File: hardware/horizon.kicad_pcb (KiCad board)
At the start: 4 copper layers, 106.9 x 56.2 mm, 62 parts, among them J1 Conn_01x02_Pin, J2 Conn_01x06_Pin, J3 USB_C_Receptacle_USB2.0_14P, J4 Conn_01x14_Pin, J5 Conn_01x02_Socket, J6 Conn_01x02_Pin, J7 SD_Card_Receptacle, Q1 NPN, SW1 SW_Push, SW2 SW_Push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

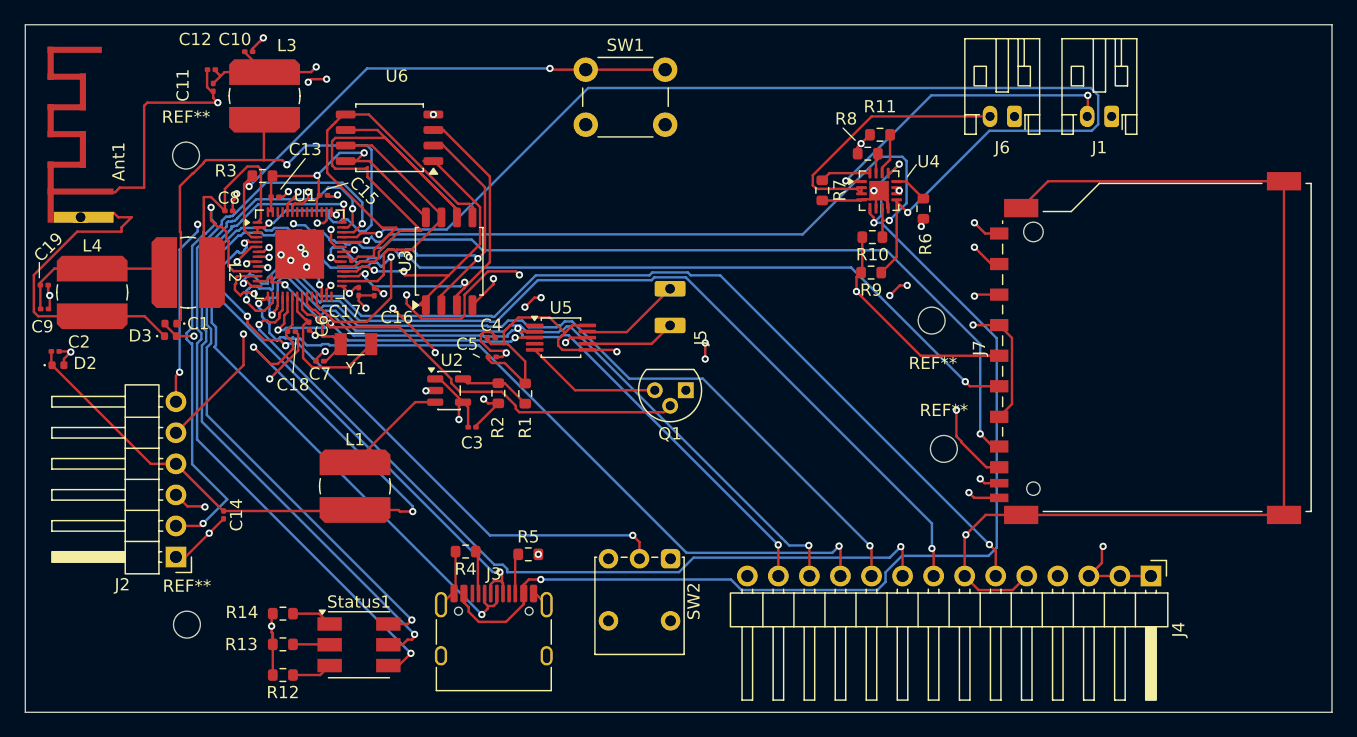
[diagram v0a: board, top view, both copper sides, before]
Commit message: Fixed connectors
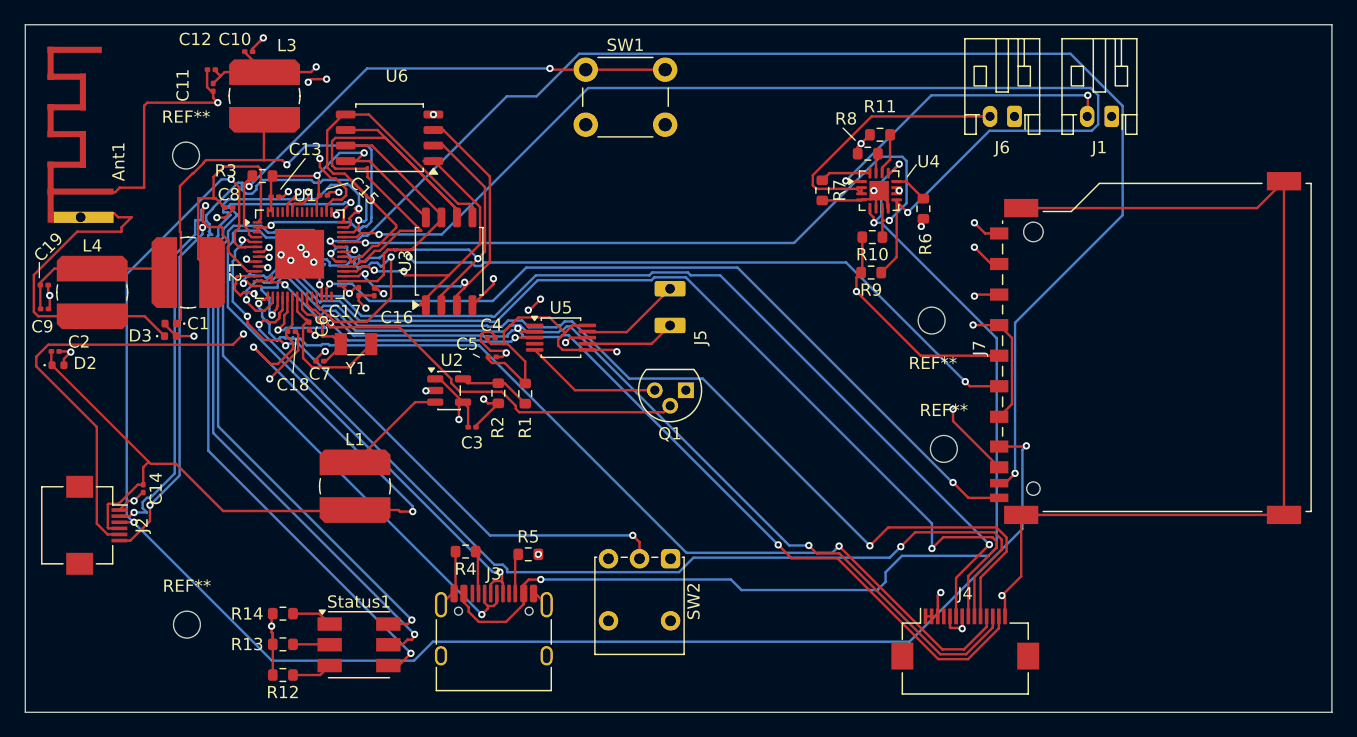
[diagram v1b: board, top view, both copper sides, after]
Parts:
- J2: footprint Connector_PinHeader_2.54mm:PinHeader_1x06_P2.54mm_Horizontal -> Connector_FFC-FPC:Hirose_FH12-6S-0.5SH_1x06-1MP_P0.50mm_Horizontal
- J4: footprint Connector_PinHeader_2.54mm:PinHeader_1x14_P2.54mm_Horizontal -> Connector_FFC-FPC:Hirose_FH12-14S-0.5SH_1x14-1MP_P0.50mm_Horizontal
- moved J4 16.0 mm to (178.5, 101.0), turned to 0 degrees
- moved J2 6.97 mm to (107.5, 91.8), turned to -90 degrees
- moved C14 6.92 mm to (111.2, 88.8)
- moved C8 0.28 mm to (118.2, 65.8)
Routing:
- net SDCARD_DAT0: track 78.5 -> 131.0 mm, vias 3 -> 2
- net +5V: track 125.1 -> 92.4 mm
- net Touch-SCL: track 18.5 -> 43.8 mm
- net SPI_HOSTHRDY: track 56.1 -> 77.5 mm
- net SPI_CLK: track 66.4 -> 84.5 mm
- net SPI_RESET: track 58.6 -> 76.6 mm
- net SPI_CS0: track 61.1 -> 75.8 mm
- net SPI_MISO: track 68.5 -> 82.4 mm
- net SPI_MOSI: track 77.5 -> 87.7 mm
- net Touch-SDA: track 24.9 -> 34.6 mm
- net SDCARD_DAT1: track 68.9 -> 78.5 mm, vias 6 -> 4
- net VDD_SPI: track 266.7 -> 273.9 mm
- net Touch-RST: track 30.5 -> 35.3 mm
- net SPI_POWERCTRL: track 79.3 -> 82.9 mm
- net Net-(Status1-BA): track 63.2 -> 66.7 mm
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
